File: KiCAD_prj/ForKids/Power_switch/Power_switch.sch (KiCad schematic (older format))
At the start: 19 parts, among them J1 Screw_Terminal_01x02, J2 Conn_01x04_Female, J3 Conn_01x04_Female, J4 Conn_01x04_Female, J5 Conn_01x04_Female, J6 Conn_01x04_Female, J7 Conn_01x04_Female, SW1 SW_SPST, U1 AMS1117-3.3, U2 AMS1117-5.0

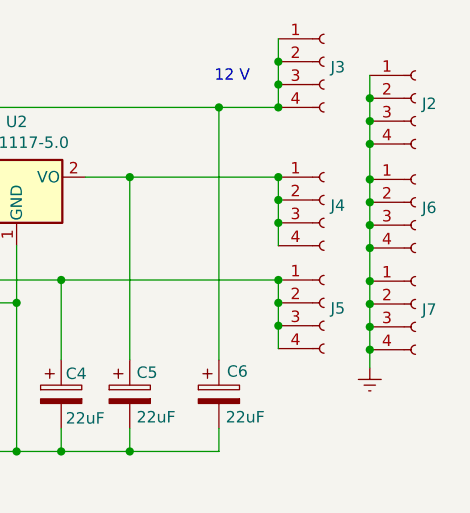
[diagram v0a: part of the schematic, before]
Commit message: Update Power Switch project KiCAD
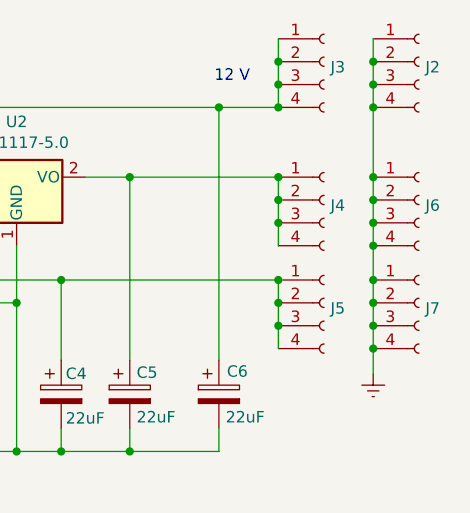
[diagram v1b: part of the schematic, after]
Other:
- moved on the sheet: J2
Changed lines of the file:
@@
 L Connector:Conn_01x04_Female J2
 U 1 1 5D4B160D
-P 7785 2695
-F 0 "J2" H 7813 2671 50  0000 L CNN
-F 1 "Conn_01x04_Female" V 7485 2540 50  0001 L CNN
-F 2 "Connector_PinHeader_2.54mm:PinHeader_1x04_P2.54mm_Vertical" H 7785 2695 50  0001 C CNN
-F 3 "~" H 7785 2695 50  0001 C CNN
-	1    7785 2695
-	1    0    0    -1
-$EndComp
-$Comp
-L Connector:Conn_01x04_Female J6
-U 1 1 5D4B914A
-P 7785 3150
-F 0 "J6" H 7813 3126 50  0000 L CNN
-F 1 "Conn_01x04_Female" V 7950 2745 50  0001 L CNN
-F 2 "Connector_PinHeader_2.54mm:PinHeader_1x04_P2.54mm_Vertical" H 7785 3150 50  0001 C CNN
-F 3 "~" H 7785 3150 50  0001 C CNN
-	1    7785 3150
+P 7800 2535
+F 0 "J2" H 7828 2511 50  0000 L CNN
+F 1 "Conn_01x04_Female" V 7500 2380 50  0001 L CNN
+F 2 "Connector_PinHeader_2.54mm:PinHeader_1x04_P2.54mm_Vertical" H 7800 2535 50  0001 C CNN
+F 3 "~" H 7800 2535 50  0001 C CNN
+	1    7800 2535
 	1    0    0    -1
 $EndComp
@@
 L Connector:Conn_01x04_Female J7
 U 1 1 5D4BA084
-P 7785 3595
-F 0 "J7" H 7813 3571 50  0000 L CNN
-F 1 "Conn_01x04_Female" V 7875 3640 50  0001 L CNN
-F 2 "Connector_PinHeader_2.54mm:PinHeader_1x04_P2.54mm_Vertical" H 7785 3595 50  0001 C CNN
-F 3 "~" H 7785 3595 50  0001 C CNN
-	1    7785 3595
-	1    0    0    -1
-$EndComp
-Wire Wire Line
-	7585 3795 7585 3695
-Connection ~ 7585 2695
-Wire Wire Line
-	7585 2695 7585 2595
-Connection ~ 7585 2795
-Wire Wire Line
-	7585 2795 7585 2695
-Connection ~ 7585 2895
-Wire Wire Line
-	7585 2895 7585 2795
-Connection ~ 7585 3050
-Wire Wire Line
-	7585 3050 7585 2895
-Connection ~ 7585 3150
-Wire Wire Line
-	7585 3150 7585 3050
-Connection ~ 7585 3250
-Wire Wire Line
-	7585 3250 7585 3150
-Connection ~ 7585 3350
-Wire Wire Line
-	7585 3350 7585 3250
-Connection ~ 7585 3495
-Wire Wire Line
-	7585 3495 7585 3350
-Connection ~ 7585 3595
-Wire Wire Line
-	7585 3595 7585 3495
-Connection ~ 7585 3695
-Wire Wire Line
-	7585 3695 7585 3595
+P 7800 3590
+F 0 "J7" H 7828 3566 50  0000 L CNN
+F 1 "Conn_01x04_Female" V 7890 3635 50  0001 L CNN
+F 2 "Connector_PinHeader_2.54mm:PinHeader_1x04_P2.54mm_Vertical" H 7800 3590 50  0001 C CNN
+F 3 "~" H 7800 3590 50  0001 C CNN
+	1    7800 3590
+	1    0    0    -1
+$EndComp
 $Comp
 L power:Earth #PWR02
 U 1 1 5D3CEC6B
-P 7585 3875
-F 0 "#PWR02" H 7585 3625 50  0001 C CNN
-F 1 "Earth" H 7585 3725 50  0001 C CNN
-F 2 "" H 7585 3875 50  0001 C CNN
-F 3 "~" H 7585 3875 50  0001 C CNN
-	1    7585 3875
-	1    0    0    -1
-$EndComp
-Wire Wire Line
-	7585 3875 7585 3795
-Connection ~ 7585 3795
+P 7600 3900
+F 0 "#PWR02" H 7600 3650 50  0001 C CNN
+F 1 "Earth" H 7600 3750 50  0001 C CNN
+F 2 "" H 7600 3900 50  0001 C CNN
+F 3 "~" H 7600 3900 50  0001 C CNN
+	1    7600 3900
+	1    0    0    -1
+$EndComp
 Wire Wire Line
 	6235 3490 7185 3490
@@
 Wire Wire Line
 	3380 4240 4235 4240
+$Comp
+L Connector:Conn_01x04_Female J6
+U 1 1 5D4B914A
+P 7800 3140
+F 0 "J6" H 7828 3116 50  0000 L CNN
+F 1 "Conn_01x04_Female" V 7965 2735 50  0001 L CNN
+F 2 "Connector_PinHeader_2.54mm:PinHeader_1x04_P2.54mm_Vertical" H 7800 3140 50  0001 C CNN
+F 3 "~" H 7800 3140 50  0001 C CNN
+	1    7800 3140
+	1    0    0    -1
+$EndComp
+Wire Wire Line
+	7600 3900 7600 3790
+Connection ~ 7600 3140
+Connection ~ 7600 3240
+Wire Wire Line
+	7600 3240 7600 3140
+Connection ~ 7600 3340
+Wire Wire Line
+	7600 3340 7600 3240
+Connection ~ 7600 3490
+Wire Wire Line
+	7600 3490 7600 3340
+Connection ~ 7600 3590
+Wire Wire Line
+	7600 3590 7600 3490
+Connection ~ 7600 3690
+Wire Wire Line
+	7600 3690 7600 3590
+Connection ~ 7600 3790
+Wire Wire Line
+	7600 3790 7600 3690
+Wire Wire Line
+	7600 2435 7600 2535
+Connection ~ 7600 2535
+Wire Wire Line
+	7600 2535 7600 2635
+Connection ~ 7600 2635
+Wire Wire Line
+	7600 2635 7600 2735
+Connection ~ 7600 2735
+Wire Wire Line
+	7600 2735 7600 3040
+Connection ~ 7600 3040
+Wire Wire Line
+	7600 3040 7600 3140
 $EndSCHEMATC
